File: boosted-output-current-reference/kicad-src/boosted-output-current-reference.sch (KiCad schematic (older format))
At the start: 15 parts, among them J1 Conn_01x02, J2 Conn_01x02, Q1 2N7002, U1 ADR425ARMZ, U2 AD8603

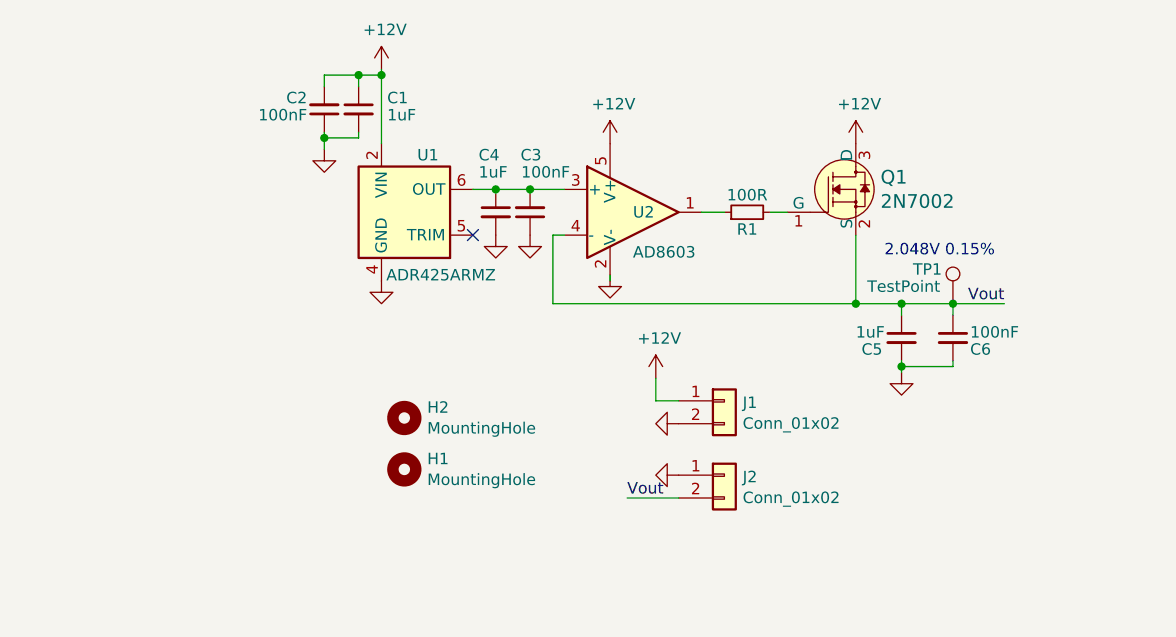
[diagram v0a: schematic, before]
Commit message: add trim to v reference
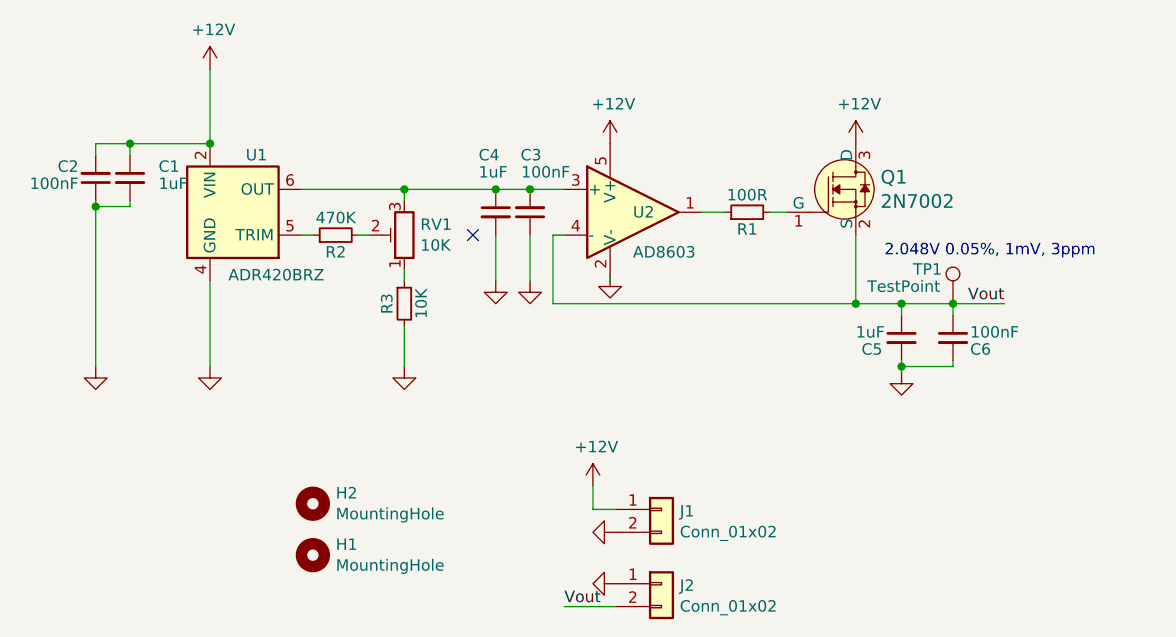
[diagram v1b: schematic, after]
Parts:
- added R2: 470K, Resistor_SMD:R_0603_1608Metric, symbol Device:R_Small
- added R3: 10K, Resistor_SMD:R_0603_1608Metric, symbol Device:R_Small
- added RV1: 10K, Potentiometer_THT:Potentiometer_Bourns_3266W_Vertical, symbol Device:R_POT_TRIM
- U1: value ADR425ARMZ -> ADR420BRZ
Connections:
- net GND: now also R3.2
- net at C3.2, C4.1, U1.6 (OUT)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: now also RV1.3
- net at U1.5 (TRIM): now also R2.1
- new net: R3.1, RV1.1
- new net: R2.2, RV1.2
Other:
- note added: "2.048V 0.05%, 1mV, 3ppm"
- note removed: "2.048V 0.15%"
- moved on the sheet: C1, C2, H1, H2, J1, J2, U1
